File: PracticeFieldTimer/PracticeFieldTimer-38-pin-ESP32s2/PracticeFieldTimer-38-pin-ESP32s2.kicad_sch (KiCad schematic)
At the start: 18 parts, among them J1 External Controls, J2 4 x 20 I2C LCD, J3 Panel, J4 DS3231 Module, J5 /CAN Enable, J6 RJ45, J7 RJ45, U1 ESP32-DevKitC

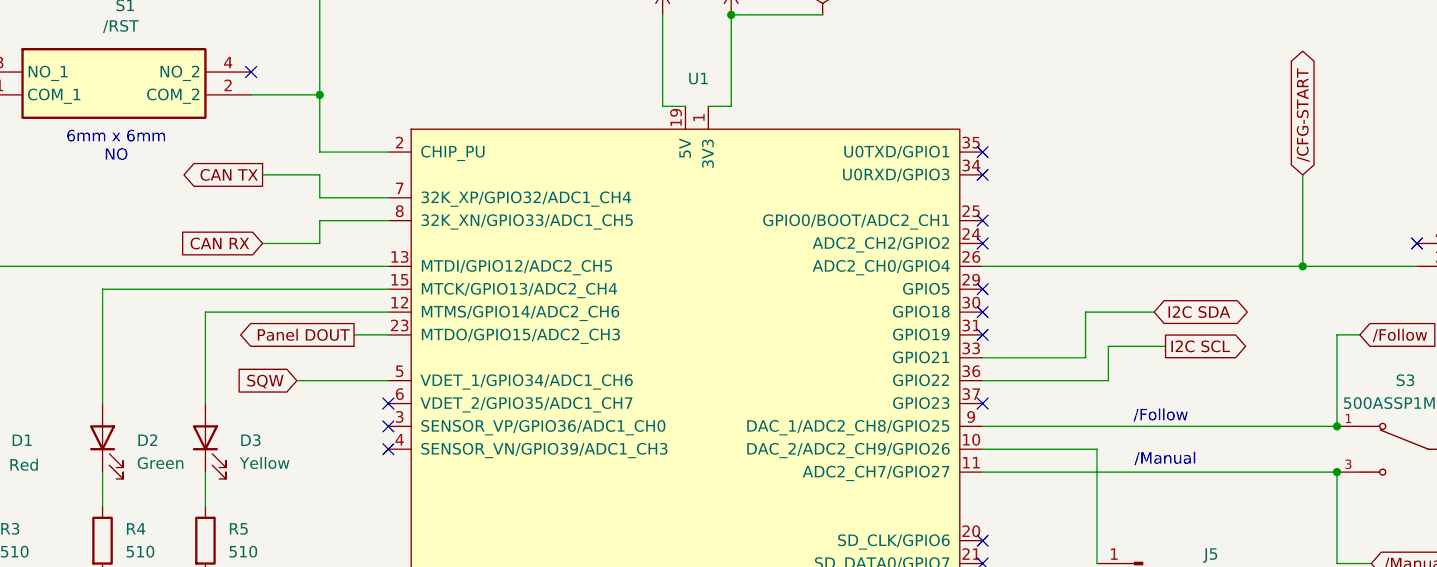
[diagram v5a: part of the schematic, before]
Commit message: Uncross CAN Transmit and CAN Receive. They were interchanged.
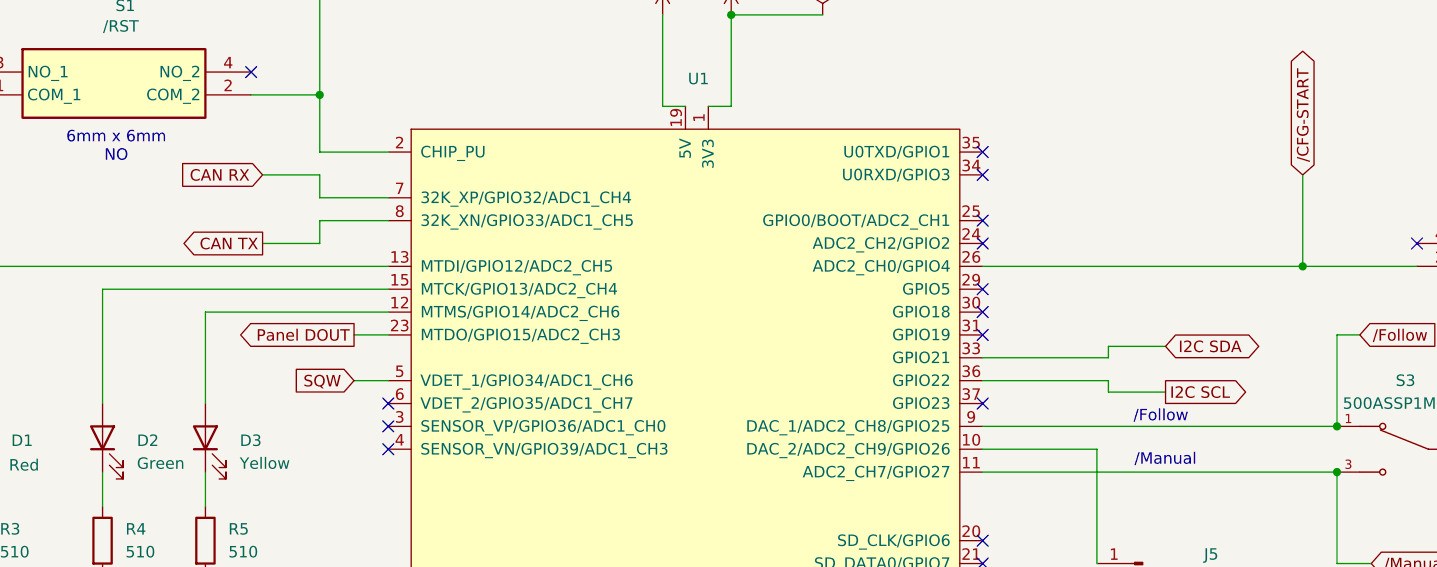
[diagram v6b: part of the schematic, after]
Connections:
- net CAN RX: now also U1.7 (32K_XP/GPIO32/ADC1_CH4); no longer U1.8 (32K_XN/GPIO33/ADC1_CH5)
- net CAN TX: now also U1.8 (32K_XN/GPIO33/ADC1_CH5); no longer U1.7 (32K_XP/GPIO32/ADC1_CH4)
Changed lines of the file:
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@@
-	(wire
-		(pts
-			(xy 93.98 77.47) (xy 87.63 77.47)
-		)
-		(stroke
-			(width 0)
-			(type default)
-		)
-	)
 	(wire
 		(pts
@@
 	(wire
 		(pts
-			(xy 91.44 100.33) (xy 101.6 100.33)
+			(xy 97.79 100.33) (xy 101.6 100.33)
 		)
 		(stroke
@@
 	(wire
 		(pts
-			(xy 167.64 97.79) (xy 179.07 97.79)
+			(xy 181.61 96.52) (xy 187.96 96.52)
 		)
 		(stroke
@@
 	(wire
 		(pts
+			(xy 181.61 96.52) (xy 181.61 97.79)
+		)
+		(stroke
+			(width 0)
+			(type default)
+		)
+	)
+	(wire
+		(pts
 			(xy 213.36 24.13) (xy 240.03 24.13)
 		)
@@
 	(wire
 		(pts
-			(xy 181.61 96.52) (xy 187.96 96.52)
+			(xy 181.61 101.6) (xy 187.96 101.6)
 		)
 		(stroke
@@
 	(wire
 		(pts
-			(xy 181.61 100.33) (xy 181.61 96.52)
+			(xy 181.61 101.6) (xy 181.61 100.33)
 		)
 		(stroke
@@
 	(wire
 		(pts
-			(xy 179.07 97.79) (xy 179.07 92.71)
-		)
-		(stroke
-			(width 0)
-			(type default)
-		)
-	)
-	(wire
-		(pts
 			(xy 220.98 149.86) (xy 233.68 149.86)
 		)
@@
 	(wire
 		(pts
-			(xy 179.07 92.71) (xy 186.69 92.71)
+			(xy 87.63 85.09) (xy 93.98 85.09)
 		)
 		(stroke
@@
 	(wire
 		(pts
-			(xy 93.98 85.09) (xy 87.63 85.09)
-		)
-		(stroke
-			(width 0)
-			(type default)
-		)
-	)
-	(wire
-		(pts
 			(xy 53.34 182.88) (xy 53.34 193.04)
 		)
@@
 	(wire
 		(pts
+			(xy 87.63 77.47) (xy 93.98 77.47)
+		)
+		(stroke
+			(width 0)
+			(type default)
+		)
+	)
+	(wire
+		(pts
 			(xy 209.55 95.25) (xy 207.01 95.25)
 		)
@@
 		(pts
 			(xy 139.7 69.85) (xy 137.16 69.85)
+		)
+		(stroke
+			(width 0)
+			(type default)
+		)
+	)
+	(wire
+		(pts
+			(xy 181.61 97.79) (xy 167.64 97.79)
 		)
 		(stroke
@@
 	(global_label "I2C SDA"
 		(shape bidirectional)
-		(at 186.69 92.71 0)
+		(at 187.96 96.52 0)
 		(fields_autoplaced yes)
 		(effects
@@
 		)
 		(property "Intersheetrefs" "${INTERSHEET_REFS}"
-			(at 198.4065 92.71 0)
+			(at 199.6765 96.52 0)
 			(effects
 				(font
@@
 	(global_label "CAN RX"
 		(shape input)
-		(at 87.63 85.09 180)
+		(at 87.63 77.47 180)
 		(fields_autoplaced yes)
 		(effects
@@
 		)
 		(property "Intersheetrefs" "${INTERSHEET_REFS}"
-			(at 77.5086 85.09 0)
+			(at 77.5086 77.47 0)
 			(effects
 				(font
@@
 	(global_label "I2C SCL"
 		(shape output)
-		(at 187.96 96.52 0)
+		(at 187.96 101.6 0)
 		(fields_autoplaced yes)
 		(effects
@@
 		)
 		(property "Intersheetrefs" "${INTERSHEET_REFS}"
-			(at 198.5047 96.52 0)
+			(at 198.5047 101.6 0)
 			(effects
 				(font
@@
 	(global_label "CAN TX"
 		(shape output)
-		(at 87.63 77.47 180)
+		(at 87.63 85.09 180)
 		(fields_autoplaced yes)
 		(effects
@@
 		)
 		(property "Intersheetrefs" "${INTERSHEET_REFS}"
-			(at 77.811 77.47 0)
+			(at 77.811 85.09 0)
 			(effects
 				(font
@@
 	(global_label "SQW"
 		(shape input)
-		(at 91.44 100.33 180)
+		(at 97.79 100.33 180)
 		(fields_autoplaced yes)
 		(effects
@@
 		)
 		(property "Intersheetrefs" "${INTERSHEET_REFS}"
-			(at 84.4634 100.33 0)
-			(effects
-				(font
+			(at 90.8134 100.33 0)
+			(effects
+				(font
